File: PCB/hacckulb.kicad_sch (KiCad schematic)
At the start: 26 parts, among them SW1 SW_Push_45deg, SW10 SW_Push_45deg, SW11 SW_Push_45deg, SW14 RotaryEncoder_Switch, SW2 SW_Push_45deg, SW3 SW_Push_45deg, SW4 SW_Push_45deg, SW5 SW_Push_45deg, SW6 SW_Push_45deg, SW7 SW_Push_45deg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

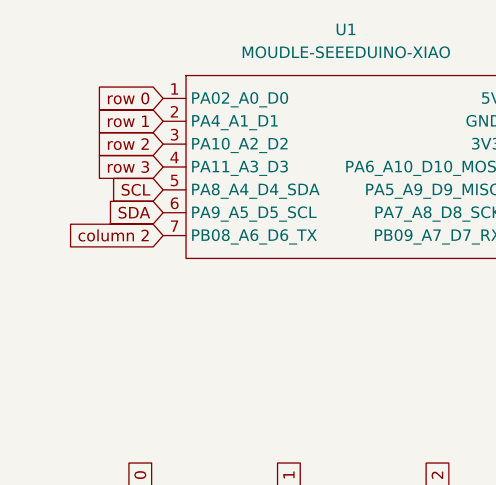
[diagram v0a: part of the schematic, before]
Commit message: updated firmware and fixed pcb (which i printed wrong :( ))
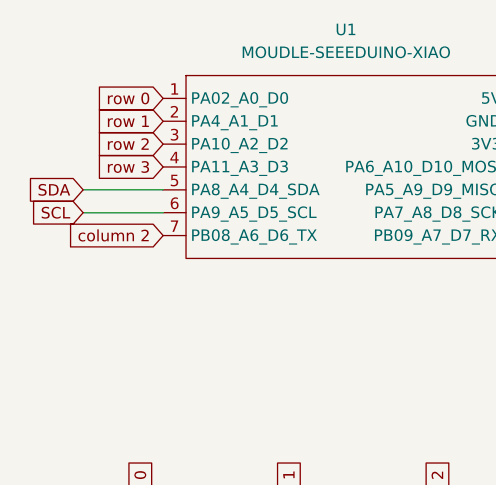
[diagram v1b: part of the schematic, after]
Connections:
- net SCL: now also U1.6 (PA9_A5_D5_SCL); no longer U1.5 (PA8_A4_D4_SDA)
- net SDA: now also U1.5 (PA8_A4_D4_SDA); no longer U1.6 (PA9_A5_D5_SCL)
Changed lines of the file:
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@@
+	(wire
+		(pts
+			(xy 40.64 52.07) (xy 49.53 52.07)
+		)
+		(stroke
+			(width 0)
+			(type default)
+		)
+	)
 	(wire
 		(pts
@@
 	(wire
 		(pts
+			(xy 40.64 54.61) (xy 49.53 54.61)
+		)
+		(stroke
+			(width 0)
+			(type default)
+		)
+	)
+	(wire
+		(pts
 			(xy 80.01 97.79) (xy 80.01 125.73)
 		)
@@
 	(global_label "SDA"
 		(shape input)
-		(at 49.53 54.61 180)
-		(fields_autoplaced yes)
-		(effects
-			(font
-				(size 1.27 1.27)
-			)
-			(justify right)
-		)
-		(property "Intersheetrefs" "${INTERSHEET_REFS}"
-			(at 42.9767 54.61 0)
+		(at 40.64 52.07 180)
+		(fields_autoplaced yes)
+		(effects
+			(font
+				(size 1.27 1.27)
+			)
+			(justify right)
+		)
+		(property "Intersheetrefs" "${INTERSHEET_REFS}"
+			(at 34.0867 52.07 0)
 			(effects
 				(font
@@
 	(global_label "SCL"
 		(shape input)
-		(at 49.53 52.07 180)
-		(fields_autoplaced yes)
-		(effects
-			(font
-				(size 1.27 1.27)
-			)
-			(justify right)
-		)
-		(property "Intersheetrefs" "${INTERSHEET_REFS}"
-			(at 43.0372 52.07 0)
-			(effects
-				(font
+		(at 40.64 54.61 180)
+		(fields_autoplaced yes)
+		(effects
+			(font
+				(size 1.27 1.27)
+			)
+			(justify right)
+		)
+		(property "Intersheetrefs" "${INTERSHEET_REFS}"
+			(at 34.1472 54.61 0)
+			(effects
+				(font
